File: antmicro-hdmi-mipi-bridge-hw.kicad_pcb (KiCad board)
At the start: 4 copper layers, 68 x 45 mm, 121 parts, among them IC1 TLV73325PDBVT, IC2 TLV73312PDBVT, IC3 TLV73325PDBVT, IC4 TLV73312PDBVT, J1 WE_68715014522, J2 47151-1001, J3 5051101992, J4 47151-1001, J5 5051101992, U1 TC358742XBG, U2 TPD8S009DSMR, U3 PCA9517ATP, U4 TC358742XBG, U5 TPD8S009DSMR, U6 PCA9517ATP, Y1 7C-27.000MBB-T, Y2 7C-27.000MBB-T

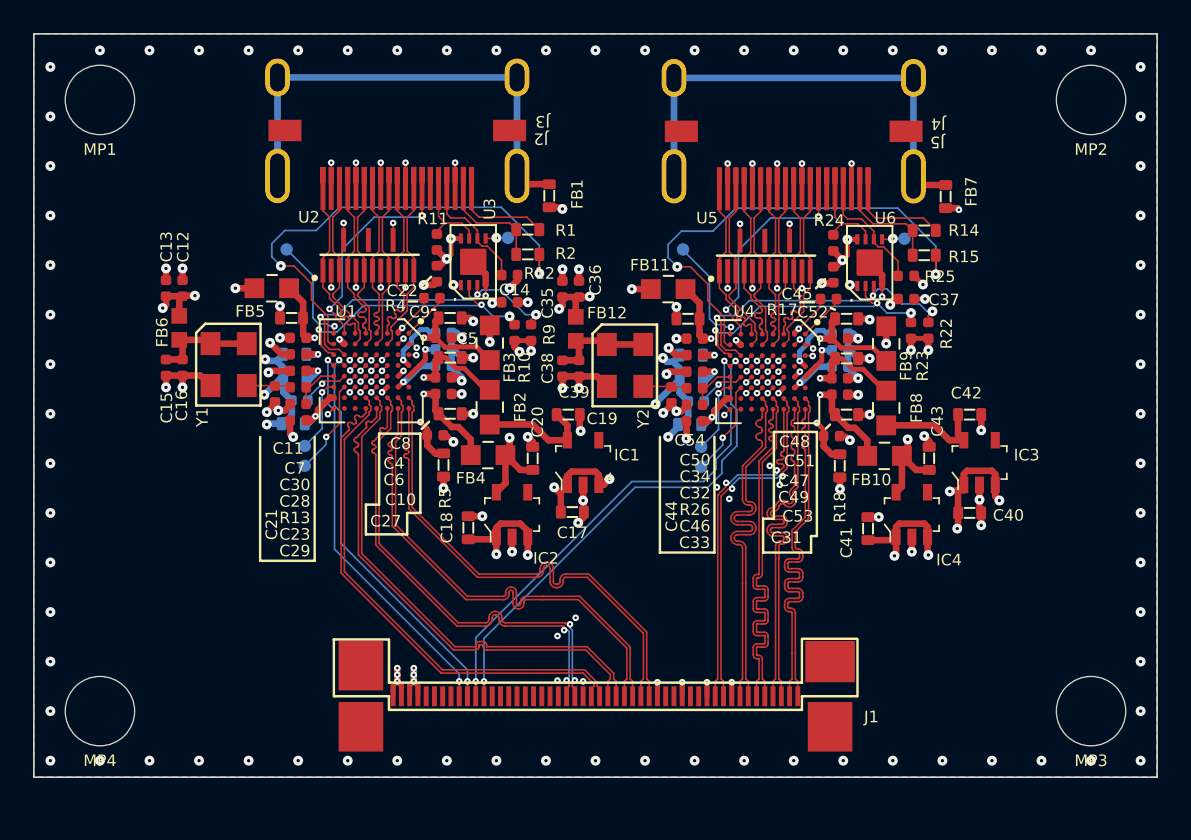
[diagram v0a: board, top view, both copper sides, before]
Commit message: Added logos
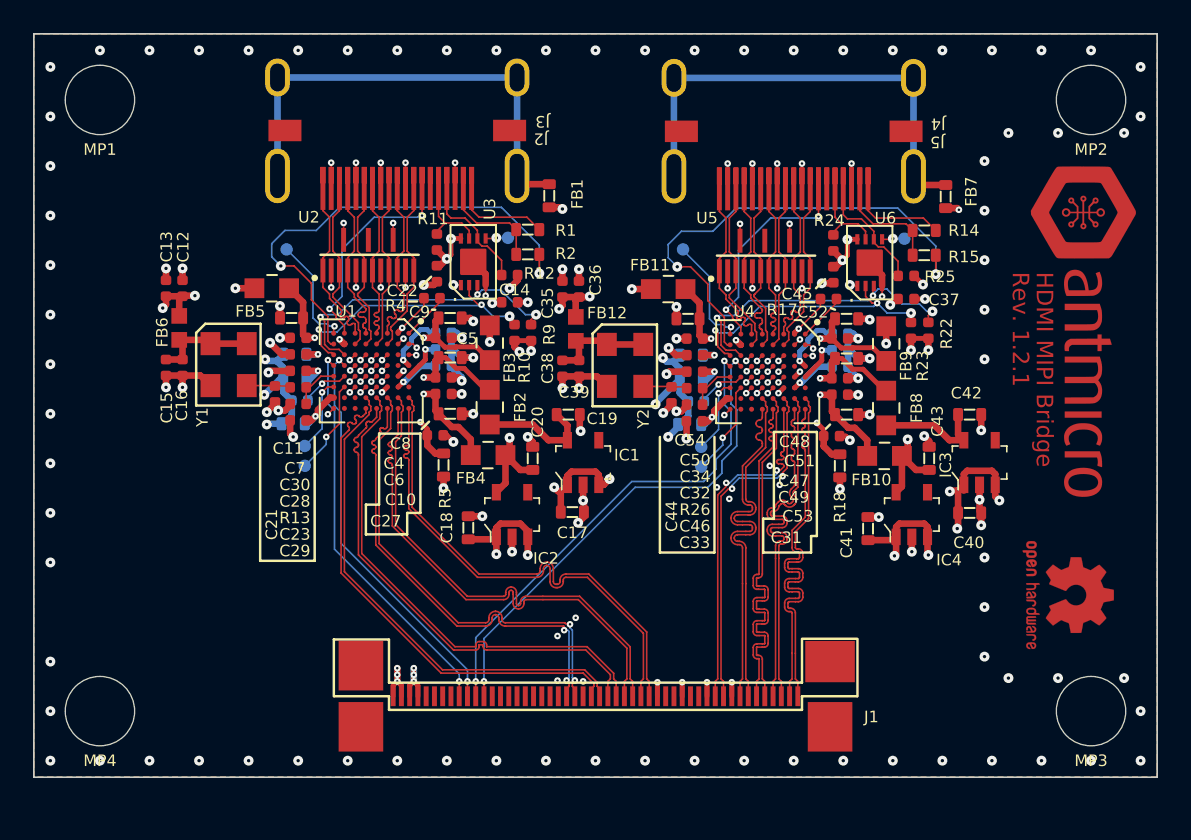
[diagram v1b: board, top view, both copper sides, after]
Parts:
- added G***: antmicro-logo_scaled_20mm, antmicro-footprints:antmicro-logo_scaled_20mm, F.Cu at (178.3, 108.0)
- added REF**: OSHW-Logo2_7.3x6mm_Copper_Mask, antmicro-footprints:OSHW-Logo2_7.3x6mm_Copper_Mask, F.Cu at (177.6, 124.0)
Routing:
- net GND: vias 182 -> 184
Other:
- board text added: "HDMI MIPI Bridge"
- board text added: "Rev. 1.2.1"

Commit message: Revision bump to 1.3.0
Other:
- board text added: "Rev. 1.3.0"
- board text removed: "Rev. 1.2.1"
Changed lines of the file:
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@@
   )
   (paper "A4")
+  (title_block
+    (title "Antmicro HDMI-MIPI Bridge")
+    (date "2023-03-02")
+    (rev "1.3.0")
+  )
   (layers
     (0 "F.Cu" signal)
@@
   (gr_line (start 159.8 119.35) (end 159.15 119.35) (layer "F.SilkS") (width 0.15))
   (gr_rect (start 115 90) (end 183 135) (layer "Edge.Cuts") (width 0.1) (fill none))
-  (gr_text "Rev. 1.2.1" (at 174.725 104.4 270) (layer "F.Cu")
+  (gr_text "Rev. 1.3.0" (at 174.725 104.4 270) (layer "F.Cu")
     (effects (font (size 1 1) (thickness 0.15)) (justify left))
   )
@@
     (effects (font (size 1 1) (thickness 0.15)) (justify left))
   )
-  (gr_text "Rev. 1.2.1" (at 174.725 104.4 270) (layer "F.Mask")
+  (gr_text "Rev. 1.3.0" (at 174.725 104.4 270) (layer "F.Mask")
     (effects (font (size 1 1) (thickness 0.15)) (justify left))
   )

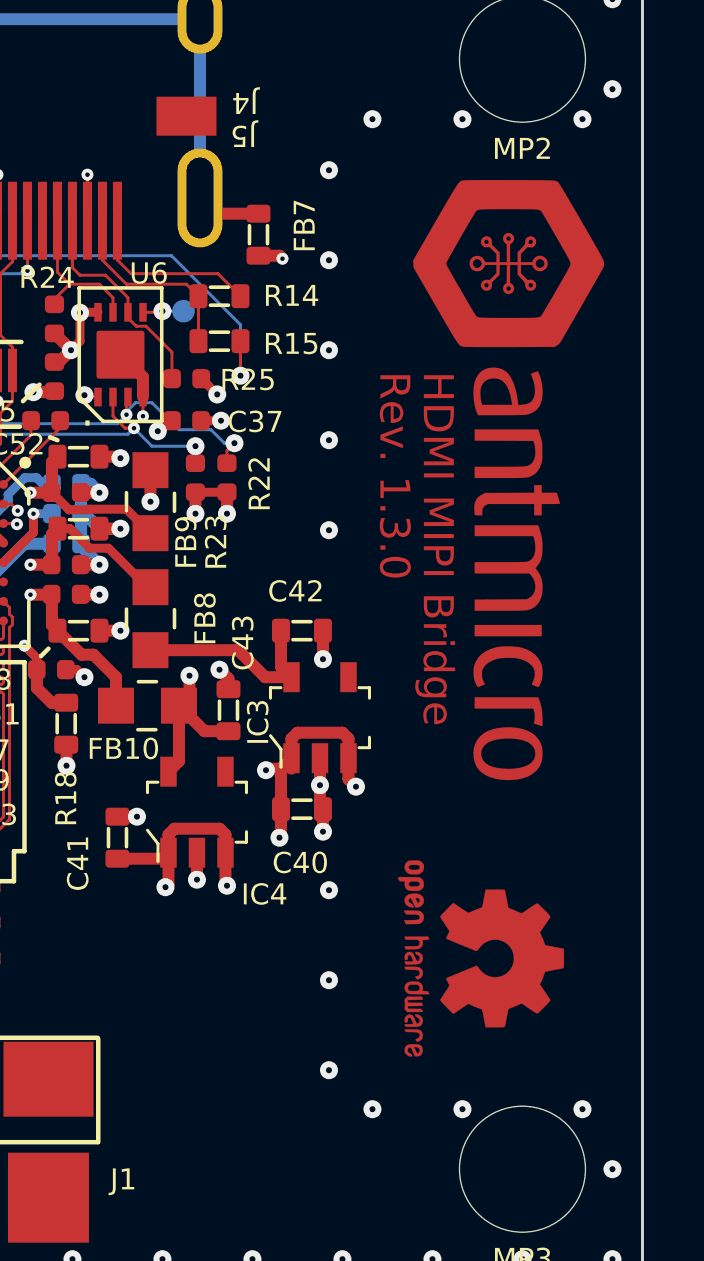
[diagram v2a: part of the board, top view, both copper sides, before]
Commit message: Fixed PCB logos
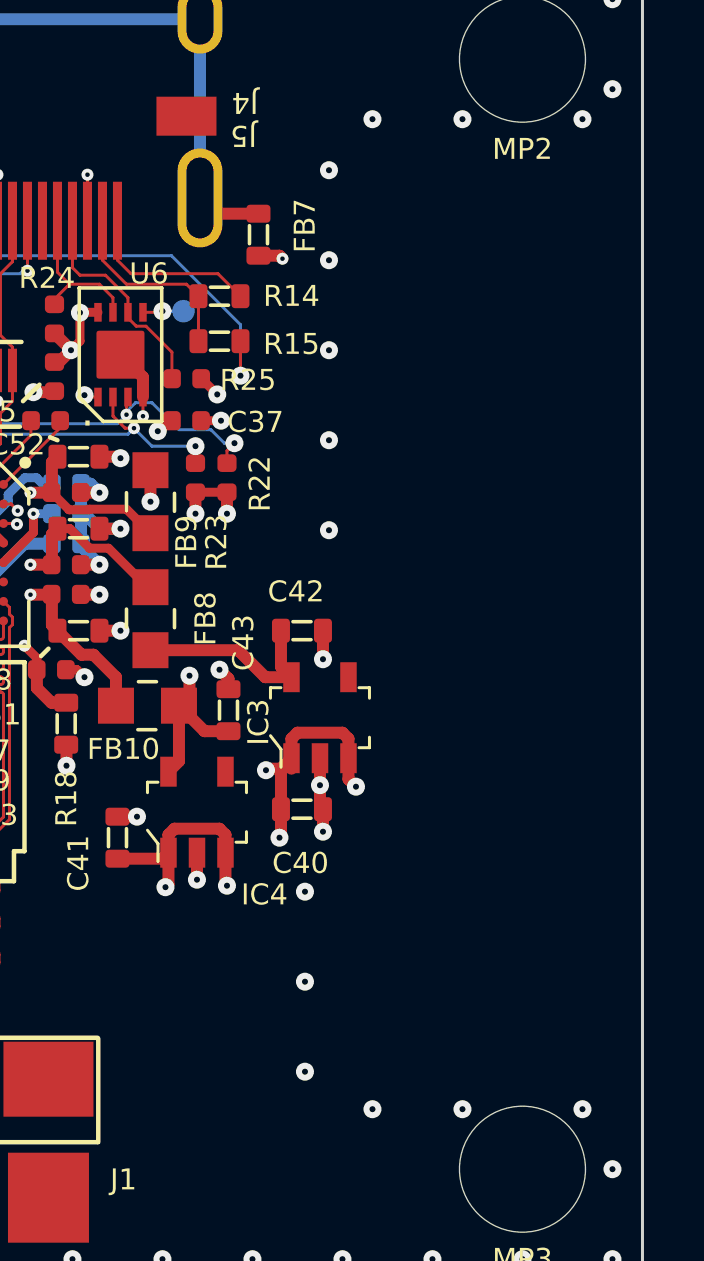
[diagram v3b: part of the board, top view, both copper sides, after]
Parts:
- removed the G*** at (178.3, 108.0)
- removed the REF** at (177.6, 124.0)
- added G***: antmicro-logo_scaled_20mm, antmicro-footprints:antmicro-logo_scaled_20mm_mask, F.Cu at (178.5, 108.0)
- added REF**: OSHW-Symbol_6.7x6mm_Copper, antmicro-footprints:OSHW-Symbol_6.7x6mm_Copper, F.Cu at (178.8, 123.2)
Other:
- board text added: "Open Hardware"

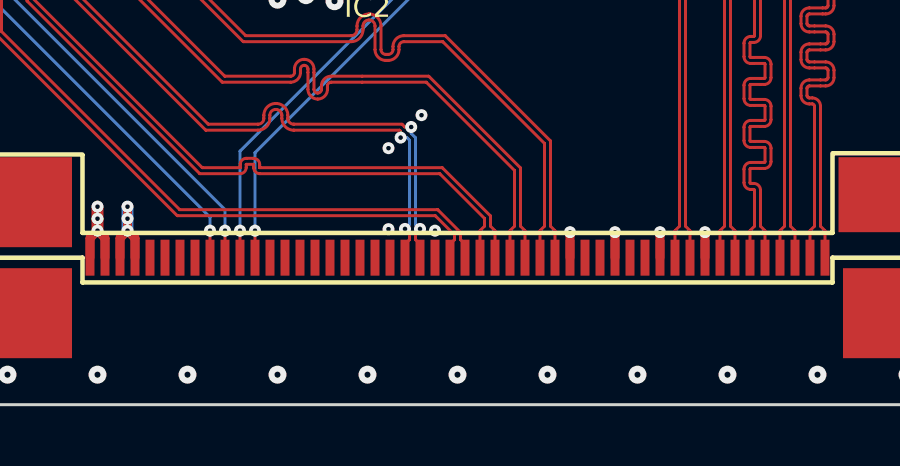
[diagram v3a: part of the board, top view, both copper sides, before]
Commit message: Added PCB SHA
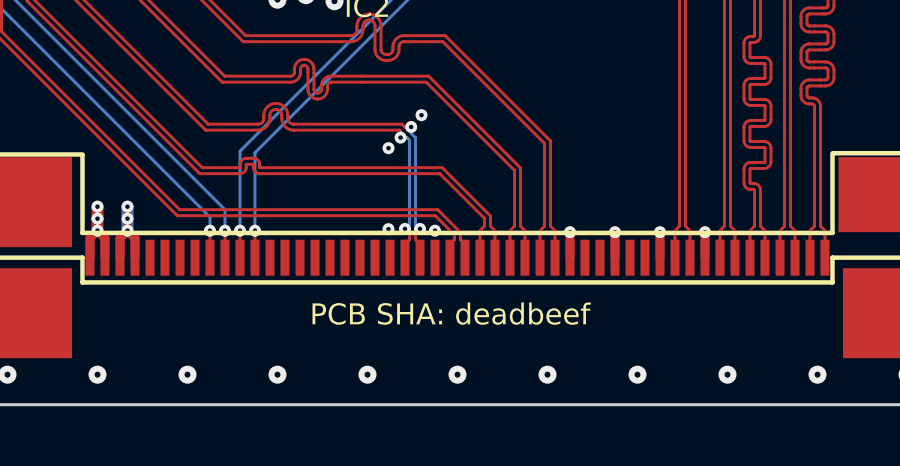
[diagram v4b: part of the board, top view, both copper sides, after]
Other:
- board text added: "PCB SHA deadbeef"
- board text added: "PCB SHA: deadbeef"
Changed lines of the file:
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@@
   (gr_line (start 159.8 119.35) (end 159.15 119.35) (layer "F.SilkS") (width 0.15))
   (gr_rect (start 115 90) (end 183 135) (layer "Edge.Cuts") (width 0.1) (fill none))
+  (gr_text "PCB SHA deadbeef" (at 149.25 162.5) (layer "B.SilkS")
+    (effects (font (size 0.65 0.65) (thickness 0.15)) (justify mirror))
+  )
+  (gr_text "PCB SHA: deadbeef" (at 148.75 132) (layer "F.SilkS")
+    (effects (font (size 0.7 0.7) (thickness 0.15)))
+  )
   (gr_text "Open\nHardware" (at 174.25 123.25 270) (layer "F.Mask")
     (effects (font (size 1 1) (thickness 0.15)))

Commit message: Updated components
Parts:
- removed J1: WE_68715014522, antmicro-footprints:WE_68715014522
- removed the REF** at (178.8, 123.2)
- added J6: WE_68715014022, antmicro-footprints:WE_68715014022, F.Cu at (148.4, 130.8)
- added REF**: OSHW-Symbol_6.7x6mm_Mask, antmicro-footprints:OSHW-Symbol_6.7x6mm_Mask, F.Cu at (178.8, 123.0)
- moved MP2 60.0 mm to (119.0, 94.0)
- moved MP4 60.0 mm to (179.0, 131.0)
- moved MP1 37.0 mm to (119.0, 131.0)
- moved MP3 37.0 mm to (179.0, 94.0)
- moved G*** 0.25 mm to (178.5, 108.2)

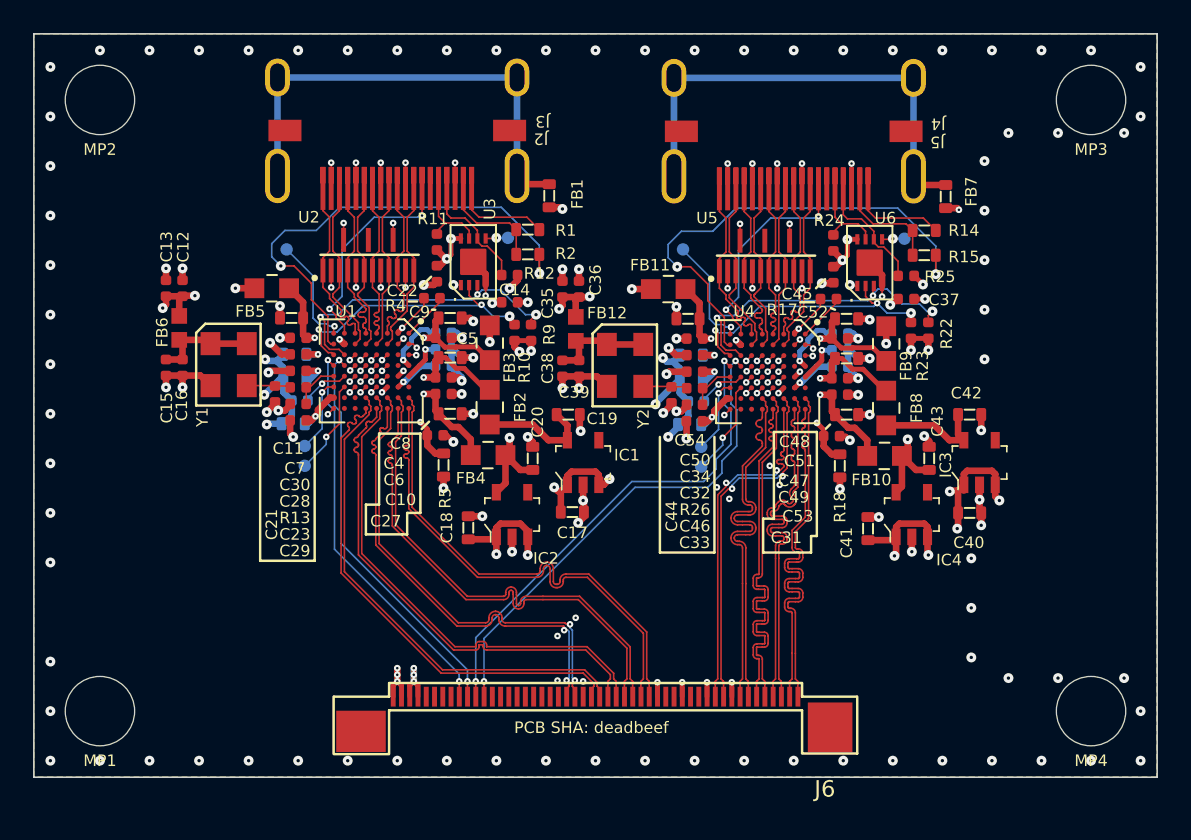
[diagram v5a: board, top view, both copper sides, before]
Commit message: Changed mounting holes to stubs
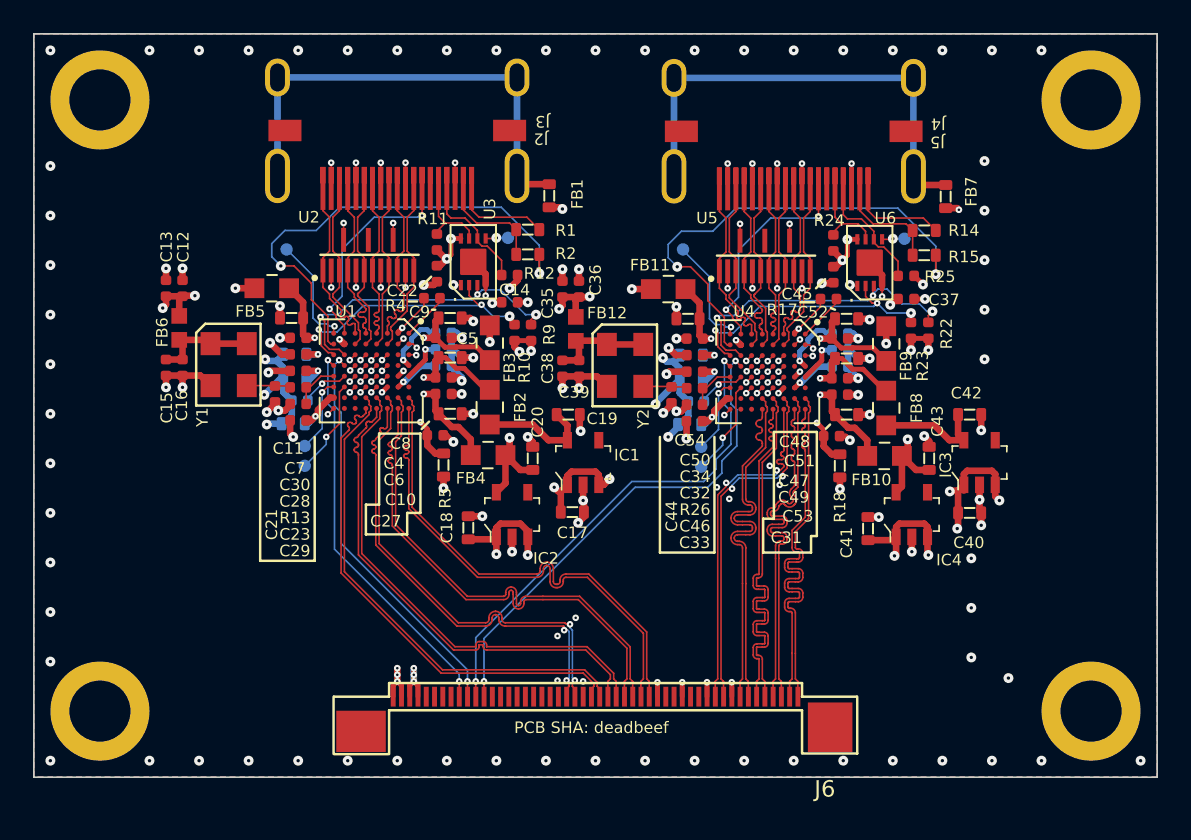
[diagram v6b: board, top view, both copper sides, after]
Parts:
- removed MP1, MP2, MP3, MP4: PCB_Mount_Hole_4.3_NPTH, antmicro-footprints:mounting-hole-4.2mm-NPTH
- added SP1: 9774060151, antmicro-footprints:9774060151, B.Cu at (119.0, 94.0)
- added SP2: 9774060151, antmicro-footprints:9774060151, B.Cu at (179.0, 94.0)
- added SP3: 9774060151, antmicro-footprints:9774060151, B.Cu at (179.0, 131.0)
- added SP4: 9774060151, antmicro-footprints:9774060151, B.Cu at (119.0, 131.0)
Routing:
- net GND: vias 184 -> 171
